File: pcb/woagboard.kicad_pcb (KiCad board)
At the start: 2 copper layers, 122.5 x 95 mm, 59 parts, among them J1 TYPE-C-31-M-12, J2 SWD, J3 TC2030, J4 nice!view, SW1 SW_Push_45deg, SW10 SW_Push_45deg, SW11 SW_Push_45deg, SW12 SW_Push_45deg, SW13 SW_Push_45deg, SW14 SW_Push_45deg, SW15 SW_Push_45deg, SW16 SW_Push_45deg, SW17 SW_Push_45deg, SW18 SW_Push_45deg, SW2 SW_Push_45deg, SW3 SW_Push_45deg, SW4 SW_Push_45deg, SW5 SW_Push_45deg, SW6 SW_Push_45deg, SW7 SW_Push_45deg, SW8 SW_Push_45deg, SW9 SW_Push_45deg, U1 E73-2G4M08S1C, U2 BQ24075RGT, U3 SRV05-4, Y1 32.768kHz

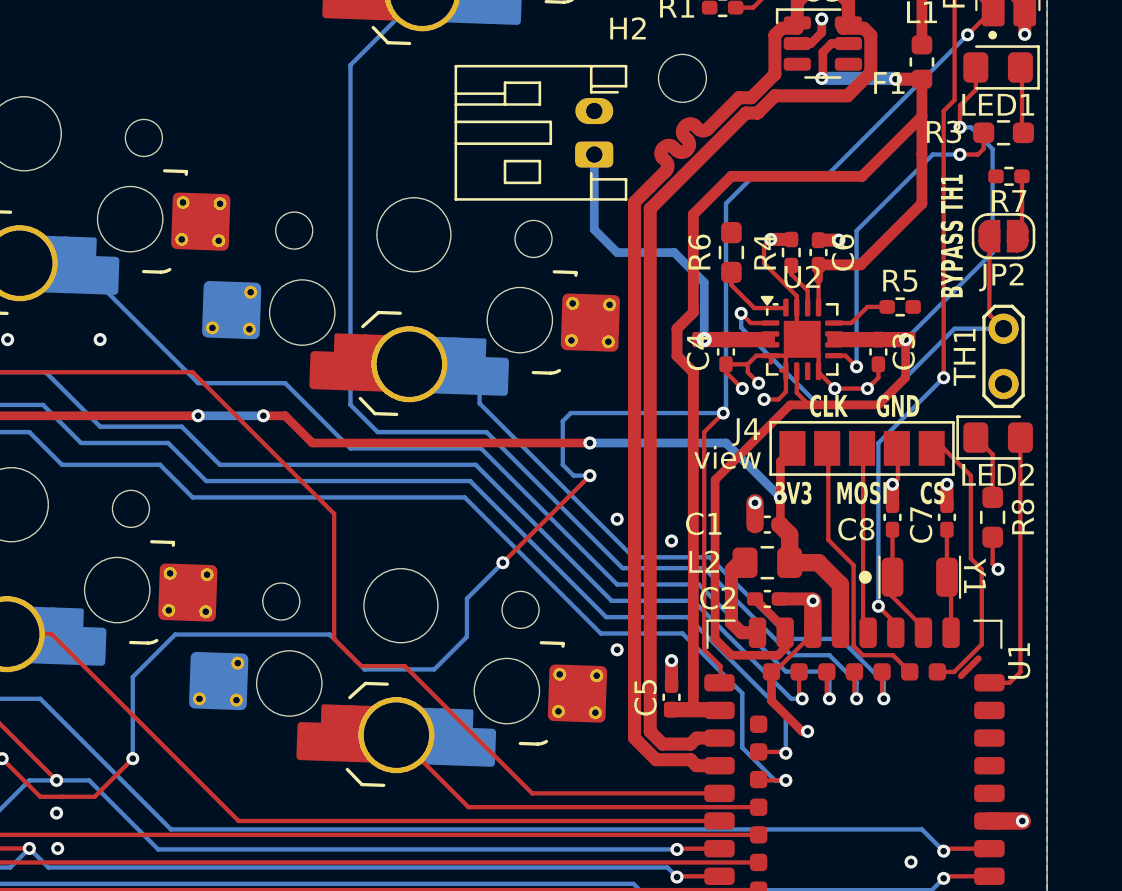
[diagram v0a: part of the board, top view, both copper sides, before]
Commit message: feat: add rust firmware
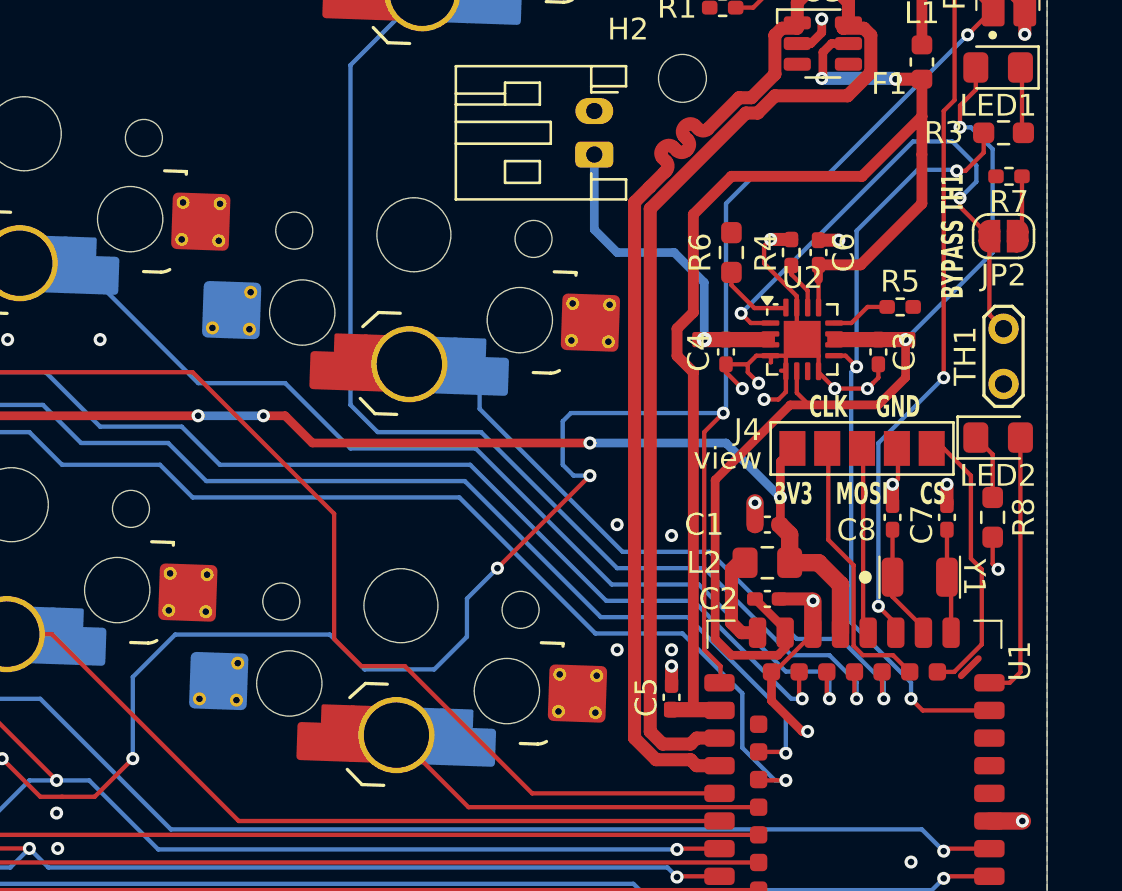
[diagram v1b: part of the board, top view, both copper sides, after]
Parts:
- removed QR*****: WobblQR, Woagboard_Footprints:WobblQR
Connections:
- R3 pad 2: /CHG -> CHG
- U1 pad 9: unconnected-(U1-P0.31/AIN7-Pad9) -> CHG
- U2 pad 9: /CHG -> CHG
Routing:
- net CHG: track 0.00 -> 36.1 mm, vias 0 -> 3
- net /CHG: track 15.7 -> 0.00 mm, vias 2 -> 0
- net TEMP: track 21.8 -> 24.9 mm, vias 1 -> 2
- net GND: track 130.7 -> 130.4 mm, vias 35 -> 36

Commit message: feat: updated production files
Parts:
- added G***: LOGO, LOGO, F.Cu at (21.0, 65.7)
- added G***: LOGO, LOGO, F.Cu at (23.9, 84.0)
- added G***: LOGO, LOGO, F.Cu at (25.8, 95.8)
- added G***: LOGO, LOGO, F.Cu at (97.6, 84.6)
- added G***: LOGO, LOGO, F.Cu at (89.4, 85.1)
- added G***: LOGO, LOGO, F.Cu at (25.4, 93.4)
- added G***: LOGO, LOGO, F.Cu at (104.3, 84.6)
- added G***: LOGO, LOGO, F.Cu at (114.8, 84.5)
- added G***: LOGO, LOGO, F.Cu at (23.2, 79.5)
- added G***: LOGO, LOGO, F.Cu at (21.4, 68.2)
- added G***: LOGO, LOGO, F.Cu at (24.3, 86.5)
- added G***: LOGO, LOGO, F.Cu at (20.3, 61.3)
- added G***: LOGO, LOGO, F.Cu at (100.9, 84.6)
- added G***: LOGO, LOGO, F.Cu at (26.3, 99.3)
- added G***: LOGO, LOGO, F.Cu at (24.7, 88.9)
- added G***: LOGO, LOGO, F.Cu at (21.7, 70.2)
- added G***: LOGO, LOGO, F.Cu at (22.8, 77.1)
- added G***: LOGO, LOGO, F.Cu at (94.2, 84.7)
- added G***: LOGO, LOGO, F.Cu at (22.1, 72.6)
- added G***: LOGO, LOGO, F.Cu at (19.5, 56.3)
- added G***: LOGO, LOGO, F.Cu at (107.8, 84.6)
- added G***: LOGO, LOGO, F.Cu at (19.9, 58.8)
- added G***: LOGO, LOGO, F.Cu at (22.5, 75.1)
- added G***: LOGO, LOGO, F.Cu at (18.7, 51.4)
- added G***: LOGO, LOGO, F.Cu at (41.6, 66.0)
- added G***: LOGO, LOGO, F.Cu at (25.9, 96.8)
- added G***: LOGO, LOGO, B.Cu at (128.0, 97.7)
- added G***: LOGO, LOGO, B.Cu at (127.9, 84.3)
- added G***: LOGO, LOGO, B.Cu at (45.8, 86.9)
- added G***: LOGO, LOGO, B.Cu at (127.7, 70.6)
- added G***: LOGO, LOGO, B.Cu at (127.8, 53.3)
- added G***: LOGO, LOGO, B.Cu at (55.8, 85.8)
- added G***: LOGO, LOGO, F.Cu at (111.4, 84.7)
- added G***: LOGO, LOGO, F.Cu at (25.0, 90.9)
- added G***: LOGO, LOGO, F.Cu at (23.6, 82.0)
- added G***: LOGO, LOGO, F.Cu at (119.2, 85.0)
- added G***: LOGO, LOGO, F.Cu at (20.6, 63.2)
- added G***: LOGO, LOGO, F.Cu at (19.1, 53.9)
- added QR*****: WobblQR, Woagboard_Footprints:WobblQR, B.Cu at (71.4, 92.0)
- moved kibuzzard-686125E5 2.24 mm to (66.0, 81.8)
- moved R7 0.75 mm to (136.0, 56.5)
- moved R8 0.33 mm to (135.2, 71.8)
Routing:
- net GND: track 130.4 -> 132.4 mm, vias 36 -> 37
- net /Bypass: track 2.83 -> 2.08 mm
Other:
- board text added: "(debubber)"
- board text added: "+BATT"
- board text added: "BYPASS"
- board text added: "Dream. Not of what you are. But of what you want to be - Space mom (Lotus), Warframe"
- board text added: "Hexagons are the bestagons"
- board text added: "JLCJLCJLCJLC"
- board text added: "LED1: CHARGE LED2: STATUS"
- board text added: "NOISE"
- board text added: "Noise is calling pick up phone"
- board text added: "PROTOCOL 3: PROTECT THE PILOT"
- board text added: "Play FFVII"
- board text added: "WOAGWOAGWOAGWOAGWOAGWOAGWOAGWO"
- board text added: "awawawawawawawawawa"
- board text added: "beep!"
- board text added: "meow!"
- board text added: "nice!view"
- board text added: "wrrf!"
- board text added: "yeag"
- board text added: "yip!"
- board text added: "{dblquote}life gave me lemons, i ate the sticker{dblquote}"
- board text removed: "BYPASS TH1"
- board text removed: "view"

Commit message: feat: add renders
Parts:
- R3: value 270Ω -> 1k5
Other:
- board text added: "{dblquote}life gave me lemons, i ate the sticker{dblquote} - Kiara Rani"
- board text removed: "{dblquote}life gave me lemons, i ate the sticker{dblquote}"
